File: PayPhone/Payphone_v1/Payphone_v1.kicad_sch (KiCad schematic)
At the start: 54 parts, among them J1 JST_05, J2 Molex_26-60-4030, J3 Molex_26-60-4040, J6 PINHD_1x5_Male, J7 PINHD_1x2_Male, K1 G6S-2, Q2 2N7000, Q3 IRF630, Q4 2N7000, Q5 2N7000, U1 MCP23008-xP, U2 MC34063AP, U3 UC3843AN

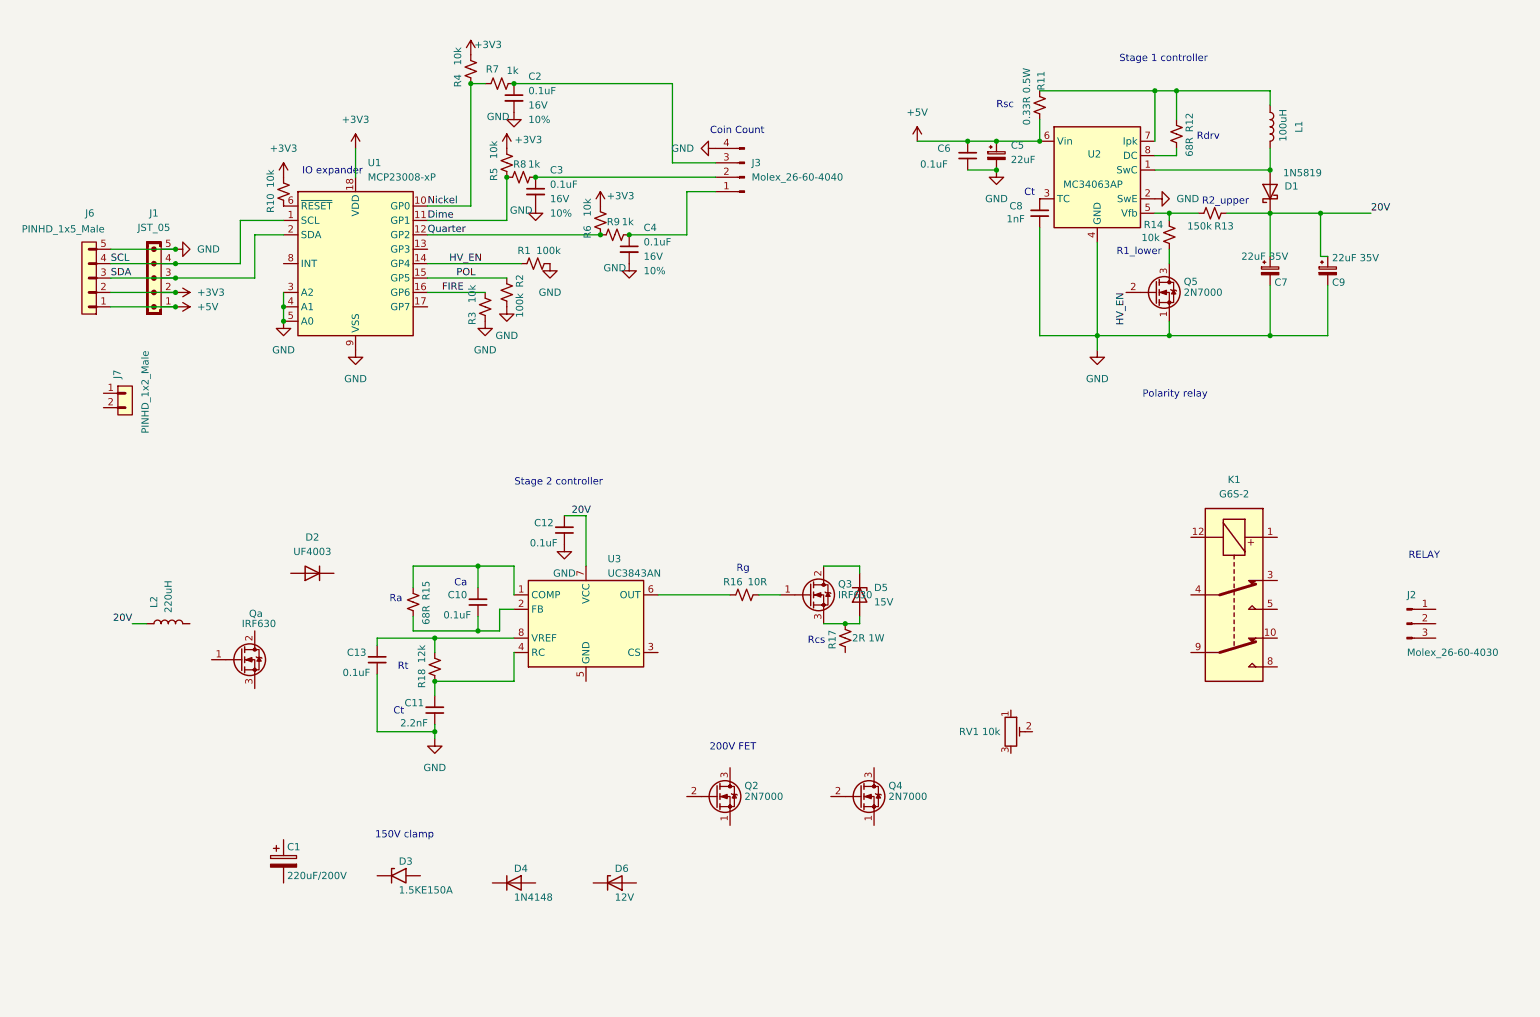
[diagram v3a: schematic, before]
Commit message: Payphone coin board schematic: through-hole footprints for all resistors and capacitors (1/4 W DIN0207, R11 0.5 W, Rcs 1 W, 5 mm ceramics, film Cz), G6S-2 footprint for K1, Cf 470 pF; Qa/Q3 swapped, Rg 100 ohm, Cslope to ISENSE
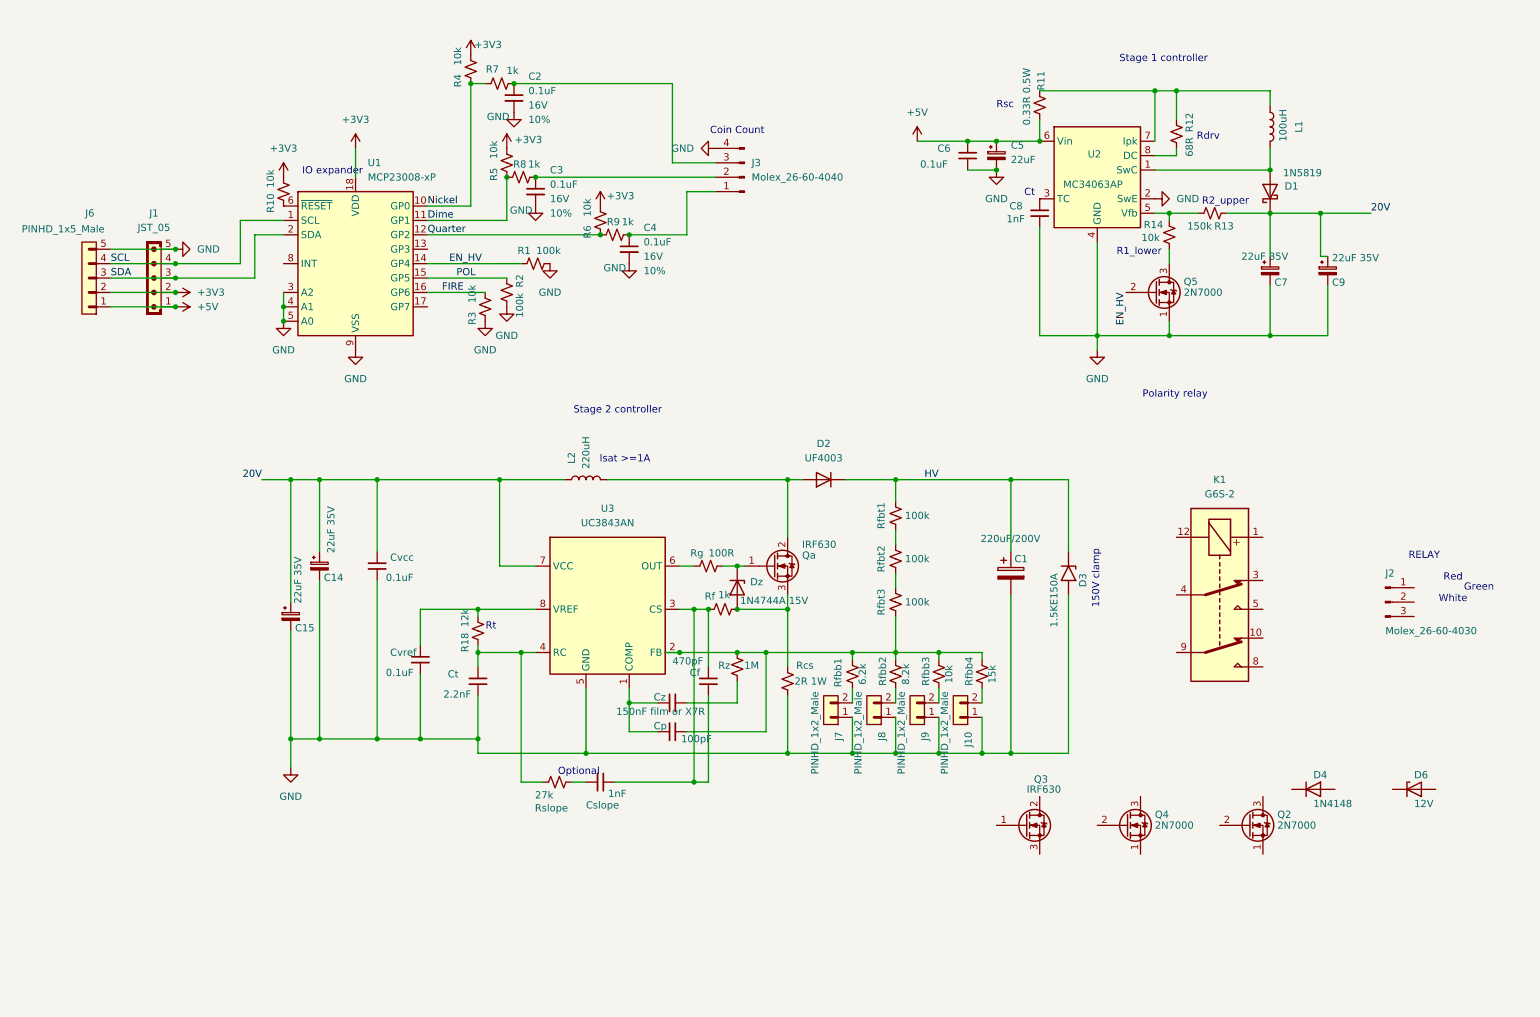
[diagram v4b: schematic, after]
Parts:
- removed C10: 0.1uF, Capacitor_THT:C_Disc_D10.0mm_W2.5mm_P5.00mm, symbol Device:C_Small
- removed R15: 68R, PCM_SparkFun-Resistor:R_0603_1608Metric, symbol PCM_SparkFun-Resistor:R_Small
- removed RV1: 10k, Potentiometer_THT:Potentiometer_Bourns_3296W_Vertical, symbol Device:R_Potentiometer_Trim
- added C14, C15: 22uF 35V, Capacitor_THT:CP_Radial_D5.0mm_P2.00mm, symbol Device:C_Polarized_Small
- added Cf: 470pF, Capacitor_THT:C_Disc_D5.0mm_W2.5mm_P5.00mm, symbol Device:C_Small
- added Cp: 100pF, Capacitor_THT:C_Disc_D5.0mm_W2.5mm_P5.00mm, symbol Device:C_Small
- added Cslope: 1nF, Capacitor_THT:C_Disc_D5.0mm_W2.5mm_P5.00mm, symbol Device:C_Small
- added Cz: 150nF film or X7R, Capacitor_THT:C_Rect_L7.2mm_W2.5mm_P5.00mm_FKS2_FKP2_MKS2_MKP2, symbol Device:C_Small
- added J10, J8, J9: PINHD_1x2_Male, Connector_PinHeader_2.54mm:PinHeader_1x02_P2.54mm_Vertical, symbol PCM_SL_Pin_Headers:PINHD_1x2_Male
- added Rf: 1k, Resistor_THT:R_Axial_DIN0207_L6.3mm_D2.5mm_P10.16mm_Horizontal, symbol PCM_SparkFun-Resistor:R_Small
- added Rfbb1: 6.2k, Resistor_THT:R_Axial_DIN0207_L6.3mm_D2.5mm_P10.16mm_Horizontal, symbol PCM_SparkFun-Resistor:R_Small
- added Rfbb2: 8.2k, Resistor_THT:R_Axial_DIN0207_L6.3mm_D2.5mm_P10.16mm_Horizontal, symbol PCM_SparkFun-Resistor:R_Small
- added Rfbb3: 10k, Resistor_THT:R_Axial_DIN0207_L6.3mm_D2.5mm_P10.16mm_Horizontal, symbol PCM_SparkFun-Resistor:R_Small
- added Rfbb4: 15k, Resistor_THT:R_Axial_DIN0207_L6.3mm_D2.5mm_P10.16mm_Horizontal, symbol PCM_SparkFun-Resistor:R_Small
- added Rfbt1, Rfbt2, Rfbt3: 100k, Resistor_THT:R_Axial_DIN0207_L6.3mm_D2.5mm_P10.16mm_Horizontal, symbol PCM_SparkFun-Resistor:R_Small
- added Rslope: 27k, Resistor_THT:R_Axial_DIN0207_L6.3mm_D2.5mm_P10.16mm_Horizontal, symbol PCM_SparkFun-Resistor:R_Small
- added Rz: 1M, Resistor_THT:R_Axial_DIN0207_L6.3mm_D2.5mm_P10.16mm_Horizontal, symbol PCM_SparkFun-Resistor:R_Small
- C2, C3, C4, C6, C8: footprint Capacitor_THT:C_Disc_D10.0mm_W2.5mm_P5.00mm -> Capacitor_THT:C_Disc_D5.0mm_W2.5mm_P5.00mm
- Ct: renamed from C11; footprint Capacitor_THT:C_Disc_D10.0mm_W2.5mm_P5.00mm -> Capacitor_THT:C_Disc_D5.0mm_W2.5mm_P5.00mm
- Cvcc: renamed from C12; footprint Capacitor_THT:C_Disc_D10.0mm_W2.5mm_P5.00mm -> Capacitor_THT:C_Disc_D5.0mm_W2.5mm_P5.00mm
- Cvref: renamed from C13; footprint Capacitor_THT:C_Disc_D10.0mm_W2.5mm_P5.00mm -> Capacitor_THT:C_Disc_D5.0mm_W2.5mm_P5.00mm
- Dz: renamed from D5; value 15V -> 1N4744A 15V
- K1: footprint (none) -> Relay_THT:Relay_DPDT_Omron_G6S-2
- R1, R10, R12, R13, R14, R18, R2, R3, R4, R5, R6: footprint PCM_SparkFun-Resistor:R_0603_1608Metric -> Resistor_THT:R_Axial_DIN0207_L6.3mm_D2.5mm_P10.16mm_Horizontal
- R11: footprint PCM_SparkFun-Resistor:R_0603_1608Metric -> Resistor_THT:R_Axial_DIN0309_L9.0mm_D3.2mm_P12.70mm_Horizontal
- R7, R8, R9: footprint PCM_SparkFun-Resistor:R_0402_1005Metric -> Resistor_THT:R_Axial_DIN0207_L6.3mm_D2.5mm_P10.16mm_Horizontal
- Rcs: renamed from R17; footprint PCM_SparkFun-Resistor:R_0603_1608Metric -> Resistor_THT:R_Axial_DIN0414_L11.9mm_D4.5mm_P15.24mm_Horizontal
- Rg: renamed from R16; value 10R -> 100R; footprint PCM_SparkFun-Resistor:R_0603_1608Metric -> Resistor_THT:R_Axial_DIN0207_L6.3mm_D2.5mm_P10.16mm_Horizontal
- U3: symbol Custom:UC3843AN -> Custom:UC3843AN-new
- renumbered Qa to Q3, Q3 to Qa
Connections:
- net 20V: now also C14.1, C15.1
- net GND: now also C1.2, D3.2 (A2), J7.1, Rcs.1, U3.5 (GND), C14.2, C15.2, J10.1, J8.1, J9.1
- net at U3.1 (COMP): now also Cp.1, Cz.1
- net at U3.2 (FB): now also Cp.2, Rfbb1.2, Rfbb2.2, Rfbb3.2, Rfbb4.2, Rfbt3.1, Rz.2
- net at U3.3 (CS): now also Cf.1, Cf.2, Cslope.1, Rf.2
- net at Ct.2, R18.2, U3.4 (RC): now also Rslope.1
- net HV: now reaches D2.1 (K)
- net HV: now also C1.1, D3.1 (A1), Rfbt1.2
- net at D2.2 (A): now also L2.2, Qa.2 (D)
- net at Dz.1 (K): now also Qa.1 (G), Rg.1; no longer Qa.2 (D)
- net at Dz.2 (A), Qa.3 (S), Rcs.2: now also Rf.1
- net at J7.2: now also Rfbb1.1
- net HV_EN renamed EN_HV
- new net: Rfbt2.1, Rfbt3.2
- new net: Rfbt1.1, Rfbt2.2
- new net: J8.2, Rfbb2.1
- new net: J10.2, Rfbb4.1
- new net: Cz.2, Rz.1
- new net: J9.2, Rfbb3.1
- new net: Cslope.2, Rslope.2
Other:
- note added: "Green"
- note added: "Isat >=1A"
- note added: "Optional"
- note added: "Red"
- note added: "White"
- note removed: "200V FET"
- note removed: "Ca"
- note removed: "Ra"
- note removed: "Rcs"
- note removed: "Rg"
- moved on the sheet: C1, Ct, Cvcc, Cvref, D2, D3, D4, D6, Dz, J2, J7, K1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
